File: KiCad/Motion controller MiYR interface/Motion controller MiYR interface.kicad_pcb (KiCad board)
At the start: 4 copper layers, 86 x 198 mm, 131 parts, among them CN1 Conn_02x40_Odd_Even, CN2 Conn_02x40_Odd_Even, J1 10061913-111PLF, J2 10061913-111PLF, J3 10061913-111PLF, J4 10061913-111PLF, J5 24v, M1 Fan, M2 Fan, U1 TPS54202DDC, U10 D1213A-04S-7, U11 D1213A-04S-7, U12 D1213A-04S-7, U13 D1213A-04S-7, U14 D1213A-04S-7, U15 D1213A-04S-7, U16 D1213A-04S-7, U17 D1213A-04S-7, U18 D1213A-04S-7, U19 D1213A-04S-7, U2 TPS54202DDC, U20 D1213A-04S-7, U21 D1213A-04S-7, U22 D1213A-04S-7, U25 TPS54202DDC, U3 D1213A-04S-7, U30 D1213A-04S-7, U31 D1213A-04S-7, U32 D1213A-04S-7, U33 D1213A-04S-7, U4 D1213A-04S-7, U5 D1213A-04S-7, U6 D1213A-04S-7, U7 D1213A-04S-7, U8 D1213A-04S-7, U9 D1213A-04S-7

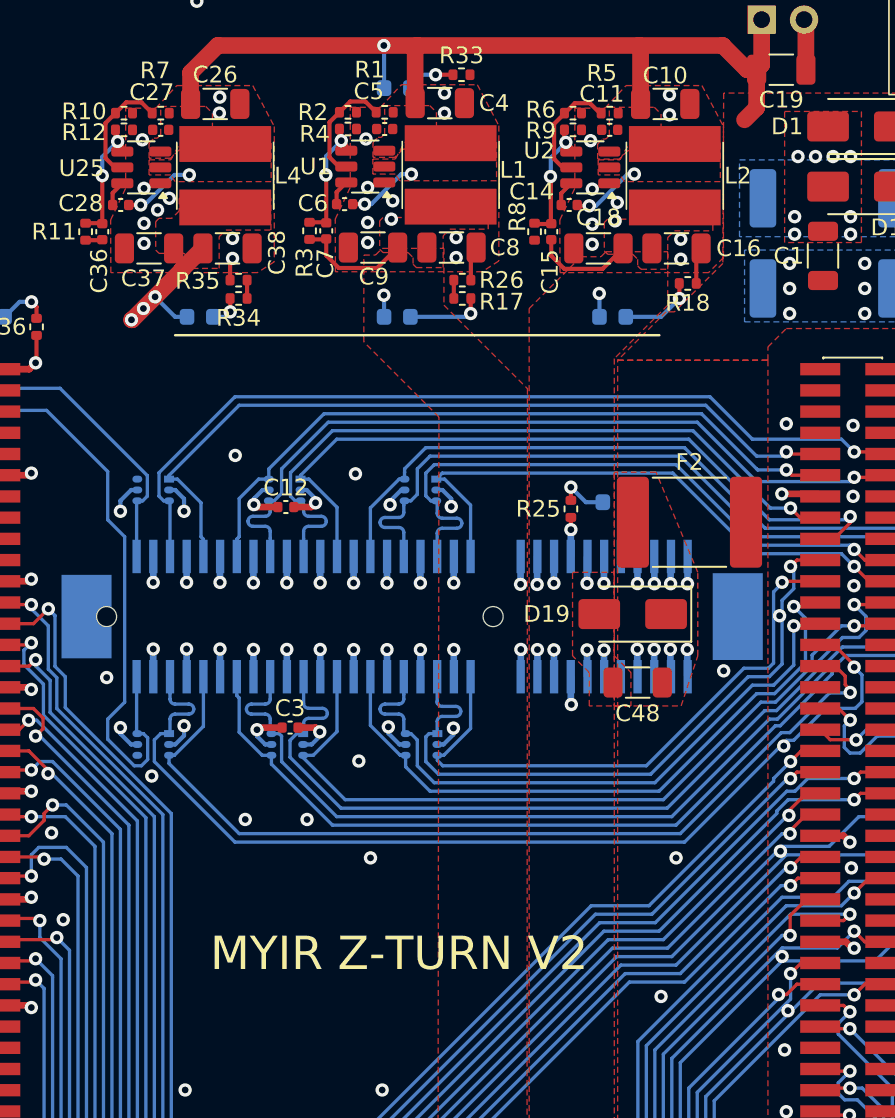
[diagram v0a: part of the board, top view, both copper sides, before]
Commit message: add modular boards
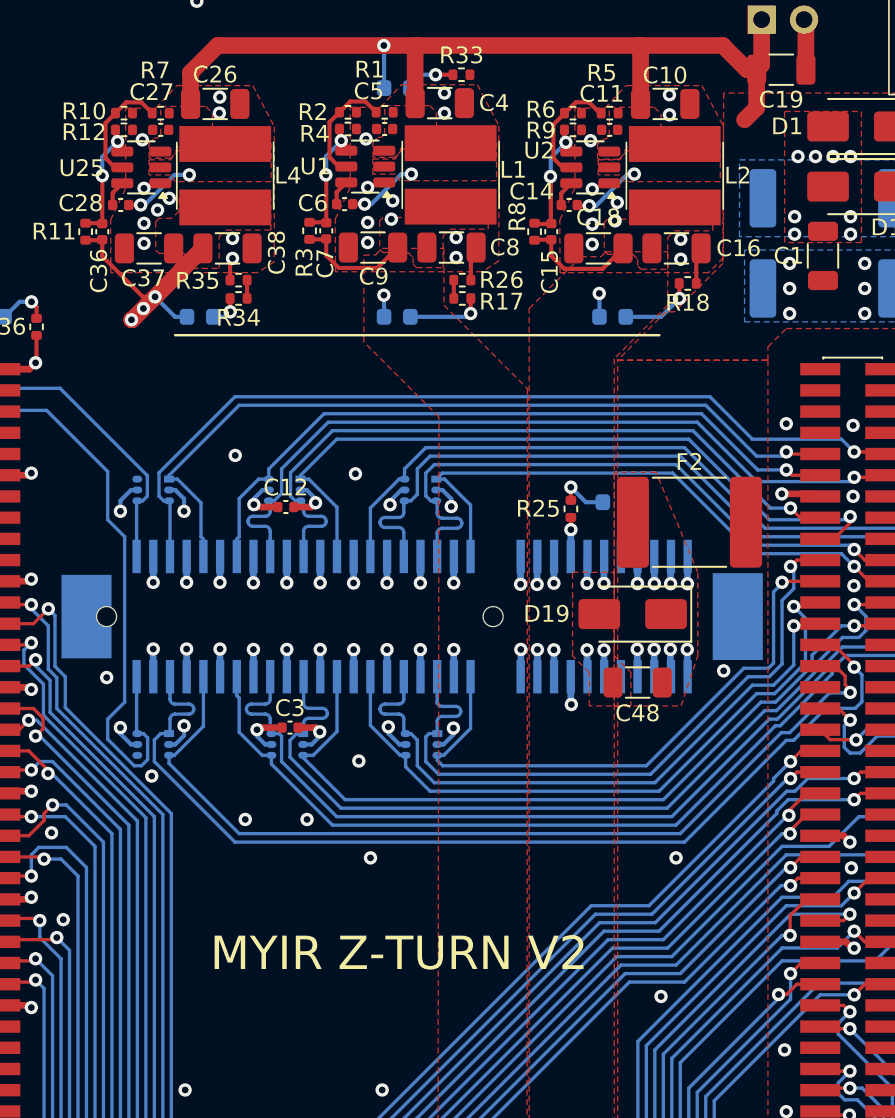
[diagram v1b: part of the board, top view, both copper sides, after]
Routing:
- net +5V: track 129.8 -> 135.0 mm
- net +3.3VA: track 20.6 -> 21.6 mm
- net GND: vias 292 -> 287
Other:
- board text added: "commit: a11e949"
- board text added: "github.com/ExcessiveOverkill/ controller-hardware-dev"
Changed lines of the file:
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@@
 		(tags "THT terminal block RND 205-00001 pitch 5mm size 10x9mm^2 drill 1.3mm pad 2.5mm")
 		(property "Reference" "J5"
-			(at 1.7 -5.9 360)
+			(at 1.7 -5.9 0)
 			(layer "F.SilkS")
 			(effects
@@
 		)
 		(property "Value" "24v"
-			(at 2.286 -8.128 360)
+			(at 2.286 -8.128 0)
 			(layer "F.Fab")
 			(effects
@@
 		)
 		(fp_text user "${REFERENCE}"
-			(at 2 -11.5 360)
+			(at 2 -11.5 0)
 			(layer "F.Fab")
 			(effects
@@
 			(layer "B.SilkS")
 		)
-		(group ""
-			(members "44289913-4311-4b26-8567-0222e1e573ca" "49acf74c-3c31-4c34-959e-f3899a9bd67f"
-				"4f500b2c-2611-4eff-921f-87a26bebe734" "a0d4da49-9efa-478f-b2aa-325f7af4f9ea"
-				"e2e19557-0db2-402d-9ec4-d8917ee13766" "e6f7dec3-1ec0-4aa1-bad5-301b835f0f2c"
-			)
-		)
 	)
 	(footprint "footprints:PCI_64_SMD_CONNECTOR"
@@
 		(layer "User.1")
 	)
+	(gr_text "commit: a11e949"
+		(at 164.35 165.55 -0)
+		(layer "B.SilkS")
+		(effects
+			(font
+				(size 1 1)
+				(thickness 0.15)
+			)
+			(justify left bottom mirror)
+		)
+	)
 	(gr_text "SLOTD 24v"
 		(at 189.9 224.4 0)
@@
 		)
 	)
+	(gr_text "github.com/ExcessiveOverkill/\ncontroller-hardware-dev"
+		(at 164.35 163.85 0)
+		(layer "B.SilkS")
+		(effects
+			(font
+				(size 1 1)
+				(thickness 0.15)
+			)
+			(justify left bottom mirror)
+		)
+	)
 	(gr_text "-  +"
 		(at 200.5 244 180)
@@
 	(segment
 		(start 179.725 69.08)
+		(end 178.755 69.08)
+		(width 0.25)
+		(layer "F.Cu")
+		(net 25)
+	)
+	(segment
+		(start 179.725 69.08)
 		(end 179.725 70.0451)
 		(width 0.25)
@@
 	)
 	(segment
+		(start 178.755 69.08)
+		(end 178.725 69.11)
+		(width 0.25)
+		(layer "F.Cu")
+		(net 25)
+	)
+	(segment
 		(start 179.725 70.0451)
 		(end 180.5049 70.825)
@@
 	)
 	(via
-		(at 193.55 112)
-		(size 0.8)
-		(drill 0.4)
-		(layers "F.Cu" "B.Cu")
-		(free yes)
-		(net 71)
-	)
-	(via
 		(at 150.5 109.8)
 		(size 0.8)
@@
 	)
 	(via
-		(at 193.9 115.25)
-		(size 0.8)
-		(drill 0.4)
-		(layers "F.Cu" "B.Cu")
-		(free yes)
-		(net 71)
-	)
-	(via
 		(at 169.88735 136.630195)
 		(size 0.8)
@@
 	)
 	(via
-		(at 193.65 99.4)
-		(size 0.8)
-		(drill 0.4)
-		(layers "F.Cu" "B.Cu")
-		(free yes)
-		(net 71)
-	)
-	(via
 		(at 155.237347 63.1)
 		(size 0.8)
@@
 	)
 	(via
-		(at 193.4 91.6)
-		(size 0.8)
-		(drill 0.4)
-		(layers "F.Cu" "B.Cu")
-		(free yes)
-		(net 71)
-	)
-	(via
 		(at 201.676 105.918)
 		(size 0.8)
@@
 	)
 	(via
-		(at 193.45 105.7)
-		(size 0.8)
-		(drill 0.4)
-		(layers "F.Cu" "B.Cu")
-		(free yes)
-		(net 71)
-	)
-	(via
 		(at 157.734 85.344)
 		(size 0.8)
@@
 	)
 	(segment
+		(start 152.837347 70.0701)
+		(end 155.267247 72.5)
+		(width 0.25)
+		(layer "F.Cu")
+		(net 75)
+	)
+	(segment
 		(start 140.716 122.174)
 		(end 140.716 123.444)
@@
 	)
 	(segment
+		(start 152.837347 69.08)
+		(end 152.837347 70.0701)
+		(width 0.25)
+		(layer "F.Cu")
+		(net 75)
+	)
+	(segment
 		(start 154.586 73.876347)
 		(end 154.623653 73.876347)
@@
 	)
 	(segment
+		(start 155.267247 72.5)
+		(end 156 72.5)
+		(width 0.25)
+		(layer "F.Cu")
+		(net 75)
+	)
+	(segment
 		(start 154.623653 73.876347)
 		(end 157.6 70.9)
@@
 	)
 	(segment
-		(start 179.895 64.245)
-		(end 180.45 64.8)
-		(width 0.25)
-		(layer "F.Cu")
-		(net 179)
-	)
-	(segment
-		(start 182.045 60.905)
-		(end 181.135 60.905)
+		(start 180.45 64.8)
+		(end 180.9 64.8)
 		(width 0.25)
 		(layer "F.Cu")
@@
 	)
 	(segment
-		(start 180.49 61.55)
-		(end 179.895 62.145)
+		(start 181.19 60.85)
+		(end 179.85 62.19)
 		(width 0.25)
 		(layer "F.Cu")
@@
 	(segment
 		(start 182.69 61.55)
-		(end 182.045 60.905)
+		(end 181.99 60.85)
 		(width 0.25)
 		(layer "F.Cu")
@@
 	)
 	(segment
-		(start 181.135 60.905)
-		(end 180.49 61.55)
+		(start 181.99 60.85)
+		(end 181.19 60.85)
 		(width 0.25)
 		(layer "F.Cu")
@@
 	)
 	(segment
-		(start 180.45 64.8)
-		(end 180.9 64.8)
+		(start 179.85 62.19)
+		(end 179.85 64.2)
 		(width 0.25)
 		(layer "F.Cu")
@@
 	)
 	(segment
-		(start 179.895 62.145)
-		(end 179.895 64.245)
+		(start 179.85 64.2)
+		(end 180.45 64.8)
 		(width 0.25)
 		(layer "F.Cu")
